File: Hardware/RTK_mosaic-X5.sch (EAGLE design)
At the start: 244 parts, among them J2 MAGJACK-POE, J3 MICRO-SD-PUSH-PUSH-EXT-PIN, J4 Vertical Qwiic Connector, J9 MAGJACK-POE, U1 ESP32-WROVER-IE, U10 POE_PSU-DP990X, U11 SN74AVC4T774PW, U17 URB2405YMD, U2 CH340C, U3 AP7361C-33FGEUDFN-8, U4 TXS0108, U5 TXS0108, U6 AP7361C-33FGEUDFN-8, U7 KSZ8041NL, U8 MOSAIC-X5X5, U9 KSZ8041NL

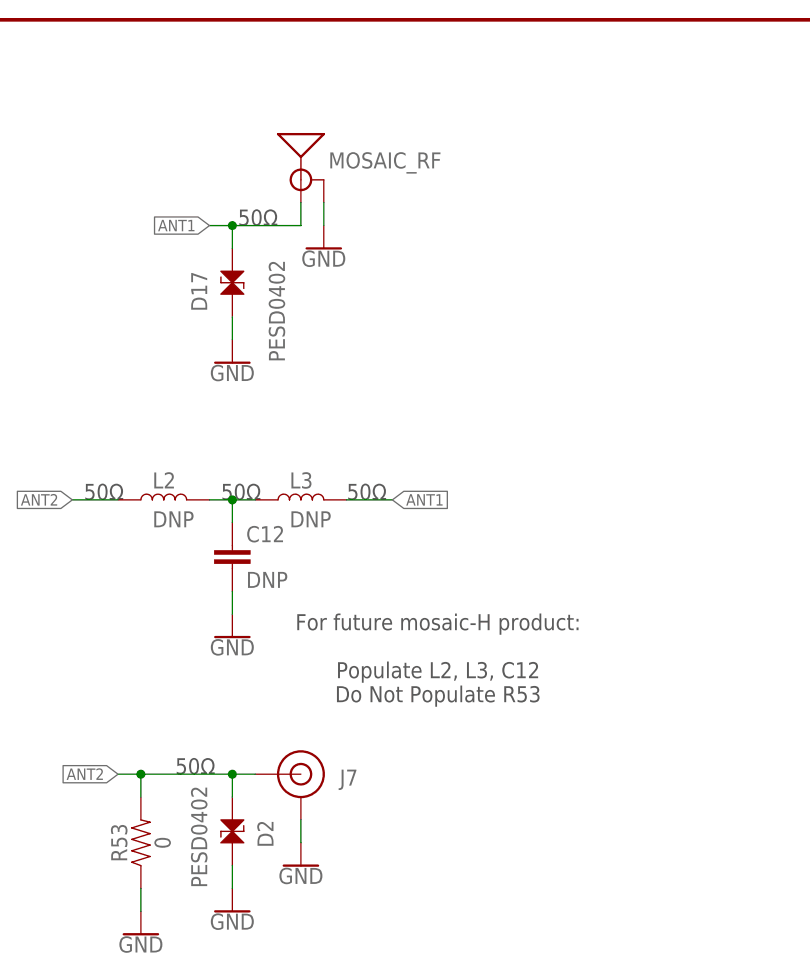
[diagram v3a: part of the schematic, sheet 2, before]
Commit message: Adding u.FL connector for mosaic-H - with standoff holes for a u.FL-SMA daughter board
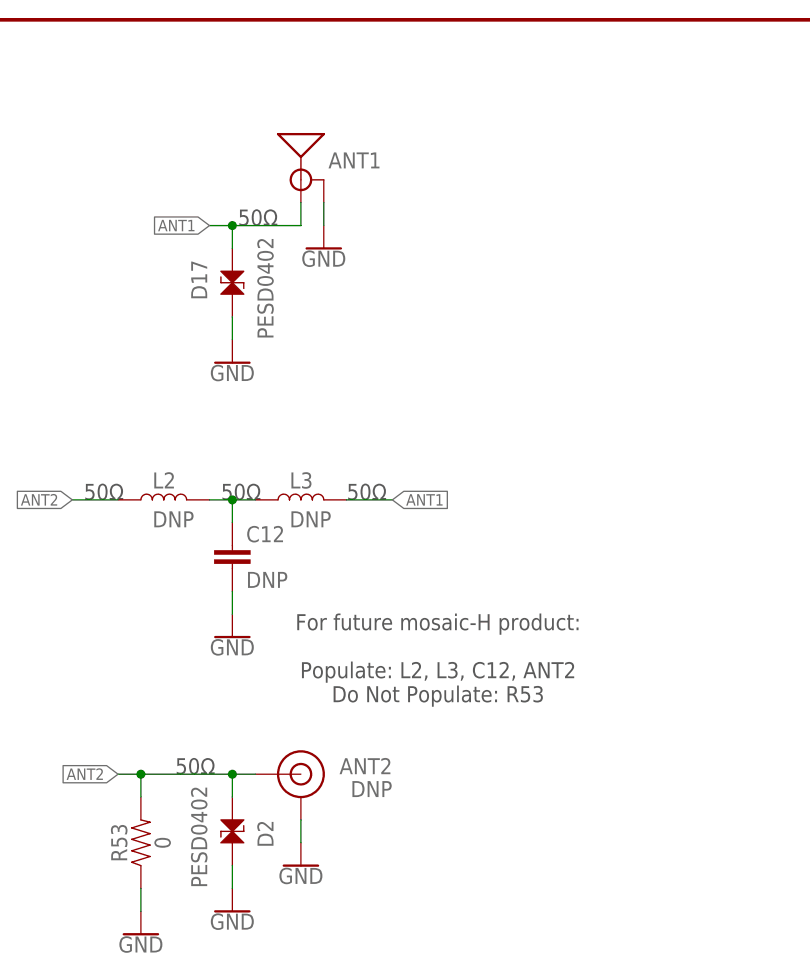
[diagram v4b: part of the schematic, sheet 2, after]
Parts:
- removed J7: (no value), SparkFun-Connectors:U.FL2PIN-REDUCED-FOOTPRINT
- added ANT2: DNP, SparkFun-Connectors:U.FL2PIN-REDUCED__DNP_NO_CREAM
- renumbered MOSAIC_RF to ANT1
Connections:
- net N$6 renamed VANT
- net ANT2: now also ANT2.SIGNAL; no longer J7.SIGNAL
- net GND: now also ANT2.GND; no longer J7.GND
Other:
- note added: "For future mosaic-H product: Populate: L2, L3, C12, ANT2 Do Not Populate: R53"
- note removed: "For future mosaic-H product: Populate L2, L3, C12 Do Not Populate R53"
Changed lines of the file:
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@@
 <part name="GND100" library="SparkFun-PowerSymbols" deviceset="GND" device=""/>
 <part name="GND99" library="SparkFun-PowerSymbols" deviceset="GND" device=""/>
-<part name="MOSAIC_RF" library="SparkFun-RF" deviceset="ANTENNA-SMA-GROUNDED" device="EDGE_SMA" value="ANTENNA-SMA-GROUNDEDEDGE_SMA"/>
+<part name="ANT1" library="SparkFun-RF" deviceset="ANTENNA-SMA-GROUNDED" device="EDGE_SMA" value="ANTENNA-SMA-GROUNDEDEDGE_SMA"/>
 <part name="D17" library="SparkFun-DiscreteSemi" deviceset="PESD0402" device="-0402" value="PESD0402"/>
 <part name="GND101" library="SparkFun-PowerSymbols" deviceset="GND" device=""/>
@@
 <part name="R52" library="SparkFun-Resistors" deviceset="0OHM" device="-0603-1/10W" value="0"/>
 <part name="1V8" library="SparkFun-Connectors" deviceset="TEST-POINT" device="POGO_PTH" value="TEST-POINTPOGO_PTH"/>
-<part name="J7" library="SparkFun-Connectors" deviceset="U.FL2PIN" device="-REDUCED-FOOTPRINT"/>
+<part name="ANT2" library="SparkFun-Connectors" deviceset="U.FL2PIN" device="-REDUCED__DNP_NO_CREAM" value="DNP"/>
 <part name="GND91" library="SparkFun-PowerSymbols" deviceset="GND" device=""/>
 <part name="D2" library="SparkFun-DiscreteSemi" deviceset="PESD0402" device="-0402" value="PESD0402"/>
@@
 <attribute name="NAME" x="193.548" y="270.51" size="1.778" layer="95" font="vector"/>
 </instance>
-<instance part="J8" gate="G$1" x="175.26" y="264.16" smashed="yes">
+<instance part="J8" gate="J1" x="175.26" y="264.16" smashed="yes">
 <attribute name="NAME" x="170.18" y="259.08" size="1.778" layer="95"/>
 <attribute name="VALUE" x="177.8" y="256.54" size="1.778" layer="96"/>
@@
 </segment>
 <segment>
-<pinref part="J8" gate="G$1" pin="GND"/>
+<pinref part="J8" gate="J1" pin="GND"/>
 <pinref part="GND59" gate="1" pin="GND"/>
 <wire x1="175.26" y1="259.08" x2="175.26" y2="256.54" width="0.1524" layer="91"/>
@@
 <net name="ESP32_RF" class="0">
 <segment>
-<pinref part="J8" gate="G$1" pin="SIGNAL"/>
+<pinref part="J8" gate="J1" pin="SIGNAL"/>
 <pinref part="ESP32_RF" gate="G$1" pin="SIGNAL"/>
 <wire x1="180.34" y1="264.16" x2="182.88" y2="264.16" width="0.1524" layer="91"/>
@@
 <text x="297.18" y="226.06" size="1.778" layer="97" font="vector">50Ω</text>
 <text x="307.34" y="213.36" size="1.778" layer="97" font="vector" align="top-center">For future mosaic-H product:
-Populate L2, L3, C12
-Do Not Populate R53</text>
+Populate: L2, L3, C12, ANT2
+Do Not Populate: R53</text>
 </plain>
 <instances>
@@
 <attribute name="VALUE" x="294.64" y="253.746" size="1.778" layer="96" font="vector" rot="MR0" align="top-center"/>
 </instance>
-<instance part="MOSAIC_RF" gate="G$1" x="292.1" y="261.62" smashed="yes">
+<instance part="ANT1" gate="G$1" x="292.1" y="261.62" smashed="yes">
 <attribute name="NAME" x="295.148" y="262.89" size="1.778" layer="95" font="vector"/>
 </instance>
 <instance part="D17" gate="D1" x="284.48" y="251.46" smashed="yes" rot="MR270">
-<attribute name="NAME" x="281.686" y="251.46" size="1.778" layer="95" font="vector" rot="MR270"/>
-<attribute name="VALUE" x="288.544" y="252.73" size="1.778" layer="96" font="vector" rot="MR270" align="top-left"/>
+<attribute name="NAME" x="281.686" y="252.73" size="1.778" layer="95" font="vector" rot="MR270"/>
+<attribute name="VALUE" x="287.274" y="255.27" size="1.778" layer="96" font="vector" rot="MR270" align="top-left"/>
 </instance>
 <instance part="GND101" gate="1" x="284.48" y="241.3" smashed="yes" rot="MR0">
@@
 </instance>
 <instance part="1V8" gate="G$1" x="167.64" y="182.88" smashed="yes" rot="R180"/>
-<instance part="J7" gate="G$1" x="292.1" y="195.58" smashed="yes" rot="MR0">
-<attribute name="NAME" x="298.45" y="194.31" size="1.778" layer="95" rot="MR0"/>
-<attribute name="VALUE" x="289.56" y="187.96" size="1.778" layer="96" rot="MR0"/>
+<instance part="ANT2" gate="J1" x="292.1" y="195.58" smashed="yes" rot="MR0">
+<attribute name="NAME" x="302.26" y="195.58" size="1.778" layer="95" rot="MR0"/>
+<attribute name="VALUE" x="302.26" y="193.04" size="1.778" layer="96" rot="MR0"/>
 </instance>
 <instance part="GND91" gate="1" x="292.1" y="185.42" smashed="yes">
@@
 </segment>
 <segment>
-<pinref part="MOSAIC_RF" gate="G$1" pin="GND"/>
+<pinref part="ANT1" gate="G$1" pin="GND"/>
 <pinref part="GND99" gate="1" pin="GND"/>
 <wire x1="294.64" y1="259.08" x2="294.64" y2="256.54" width="0.1524" layer="91"/>
@@
 </segment>
 <segment>
-<pinref part="J7" gate="G$1" pin="GND"/>
+<pinref part="ANT2" gate="J1" pin="GND"/>
 <pinref part="GND91" gate="1" pin="GND"/>
 <wire x1="292.1" y1="190.5" x2="292.1" y2="187.96" width="0.1524" layer="91"/>
@@
 </segment>
 <segment>
-<pinref part="MOSAIC_RF" gate="G$1" pin="SIGNAL"/>
+<pinref part="ANT1" gate="G$1" pin="SIGNAL"/>
 <wire x1="281.94" y1="256.54" x2="284.48" y2="256.54" width="0.1524" layer="91"/>
 <wire x1="284.48" y1="256.54" x2="292.1" y2="256.54" width="0.1524" layer="91"/>
@@
 </segment>
 </net>
-<net name="N$6" class="0">
+<net name="VANT" class="0">
 <segment>
 <pinref part="FB3" gate="G$1" pin="2"/>
@@
 </segment>
 <segment>
-<pinref part="J7" gate="G$1" pin="SIGNAL"/>
+<pinref part="ANT2" gate="J1" pin="SIGNAL"/>
 <wire x1="287.02" y1="195.58" x2="284.48" y2="195.58" width="0.1524" layer="91"/>
 <wire x1="284.48" y1="195.58" x2="274.32" y2="195.58" width="0.1524" layer="91"/>

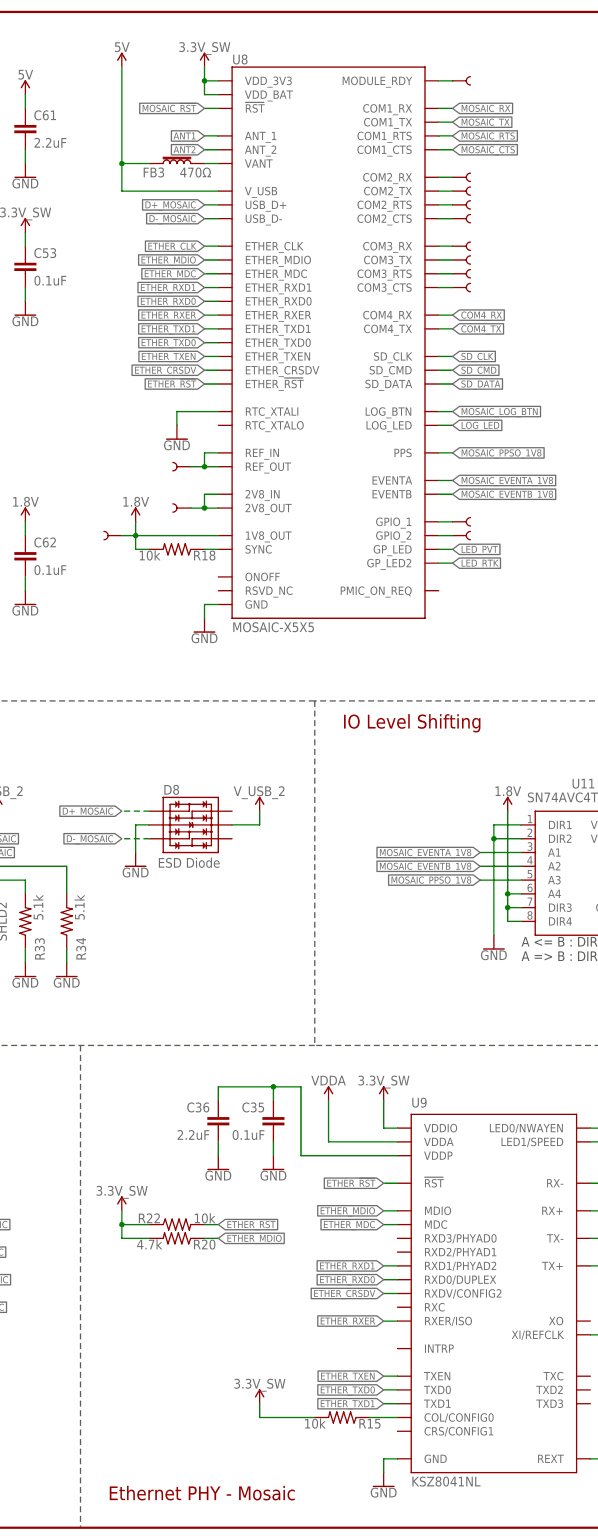
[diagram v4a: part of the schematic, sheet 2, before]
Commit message: Add Phy PROD_ID. Ready for manufacture
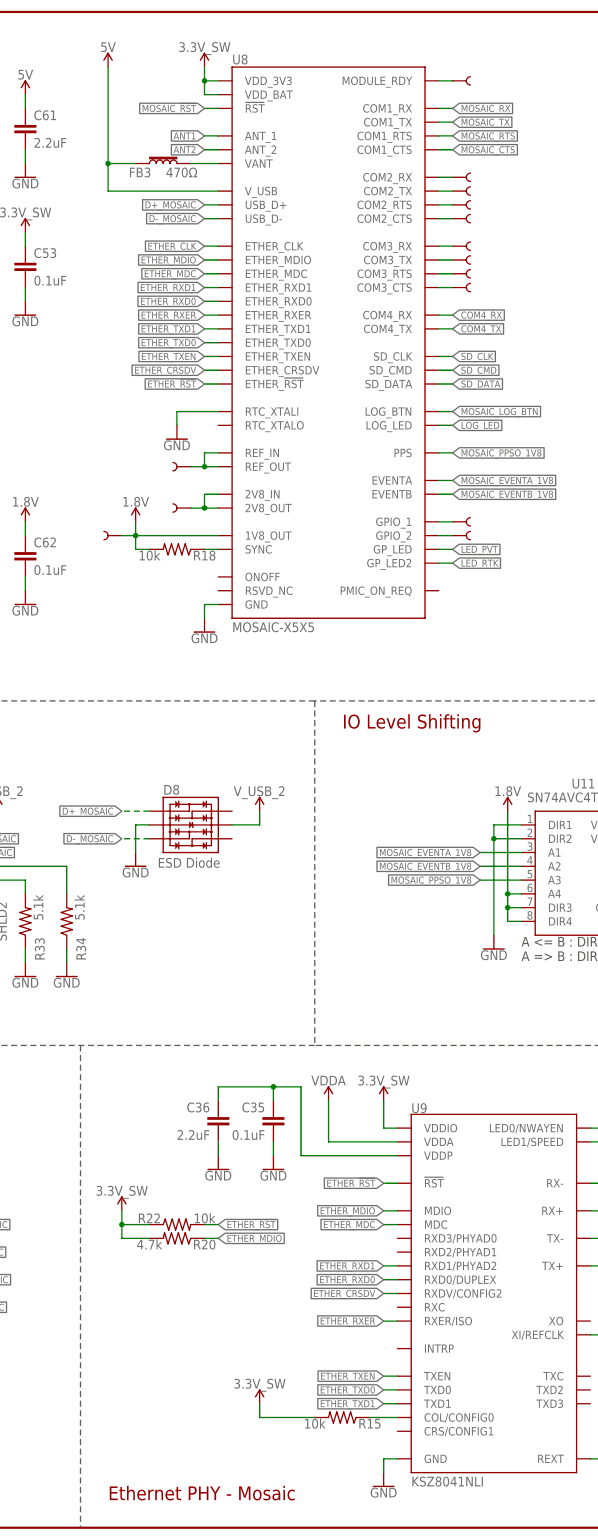
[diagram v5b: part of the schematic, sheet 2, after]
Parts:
- U7, U9: value KSZ8041NL -> KSZ8041NLI
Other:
- moved on the sheet: FB3
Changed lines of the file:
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@@
 <part name="C28" library="SparkFun-Capacitors" deviceset="0.1UF" device="-0603-25V-5%" value="0.1uF"/>
 <part name="GND62" library="SparkFun-PowerSymbols" deviceset="GND" device=""/>
-<part name="U7" library="Septentrio_mosaic-X5" deviceset="KSZ8041NL" device=""/>
+<part name="U7" library="Septentrio_mosaic-X5" deviceset="KSZ8041NL" device="" value="KSZ8041NLI"/>
 <part name="SUPPLY33" library="SparkFun-PowerSymbols" deviceset="3.3V" device=""/>
 <part name="SUPPLY38" library="SparkFun-PowerSymbols" deviceset="3.3V" device=""/>
@@
 <part name="C30" library="SparkFun-Capacitors" deviceset="0.1UF" device="-0603-25V-5%" value="0.1uF"/>
 <part name="GND41" library="SparkFun-PowerSymbols" deviceset="GND" device=""/>
-<part name="U9" library="Septentrio_mosaic-X5" deviceset="KSZ8041NL" device=""/>
+<part name="U9" library="Septentrio_mosaic-X5" deviceset="KSZ8041NL" device="" value="KSZ8041NLI"/>
 <part name="C35" library="SparkFun-Capacitors" deviceset="0.1UF" device="-0603-25V-5%" value="0.1uF"/>
 <part name="C36" library="SparkFun-Capacitors" deviceset="2.2UF" device="-0603-10V-20%" value="2.2uF"/>
@@
 </instance>
 <instance part="U7" gate="U1" x="215.9" y="78.74" smashed="yes">
-<attribute name="NAME" x="200.66" y="113.03" size="1.778" layer="95" font="vector"/>
+<attribute name="NAME" x="200.66" y="112.014" size="1.778" layer="95" font="vector"/>
 <attribute name="VALUE" x="200.66" y="43.18" size="1.778" layer="96" font="vector"/>
 </instance>
@@
 </instance>
 <instance part="U9" gate="U1" x="236.22" y="43.18" smashed="yes">
-<attribute name="NAME" x="220.98" y="77.47" size="1.778" layer="95" font="vector"/>
+<attribute name="NAME" x="220.98" y="76.454" size="1.778" layer="95" font="vector"/>
 <attribute name="VALUE" x="220.98" y="7.62" size="1.778" layer="96" font="vector"/>
 </instance>
@@
 <attribute name="VALUE" x="182.88" y="272.034" size="1.778" layer="96" align="bottom-center"/>
 </instance>
-<instance part="SUPPLY70" gate="G$1" x="167.64" y="269.24" smashed="yes">
-<attribute name="VALUE" x="167.64" y="272.034" size="1.778" layer="96" font="vector" align="bottom-center"/>
+<instance part="SUPPLY70" gate="G$1" x="165.1" y="269.24" smashed="yes">
+<attribute name="VALUE" x="165.1" y="272.034" size="1.778" layer="96" font="vector" align="bottom-center"/>
 </instance>
 <instance part="R17" gate="G$1" x="66.04" y="132.08" smashed="yes" rot="R90">
@@
 <attribute name="VALUE" x="137.16" y="188.214" size="1.778" layer="96" font="vector" align="bottom-center"/>
 </instance>
-<instance part="FB3" gate="G$1" x="177.8" y="251.46" smashed="yes" rot="R90">
-<attribute name="NAME" x="171.45" y="248.92" size="1.778" layer="95" font="vector"/>
-<attribute name="VALUE" x="184.15" y="248.92" size="1.778" layer="96" font="vector" rot="R180" align="top-left"/>
+<instance part="FB3" gate="G$1" x="175.26" y="251.46" smashed="yes" rot="R90">
+<attribute name="NAME" x="168.91" y="248.92" size="1.778" layer="95" font="vector"/>
+<attribute name="VALUE" x="181.61" y="248.92" size="1.778" layer="96" font="vector" rot="R180" align="top-left"/>
 </instance>
 <instance part="GND92" gate="1" x="149.86" y="248.92" smashed="yes">
@@
 <segment>
 <pinref part="SUPPLY70" gate="G$1" pin="5V"/>
-<wire x1="167.64" y1="246.38" x2="167.64" y2="251.46" width="0.1524" layer="91"/>
+<wire x1="165.1" y1="246.38" x2="165.1" y2="251.46" width="0.1524" layer="91"/>
 <pinref part="U8" gate="U1" pin="V_USB"/>
-<wire x1="167.64" y1="251.46" x2="167.64" y2="269.24" width="0.1524" layer="91"/>
-<wire x1="185.42" y1="246.38" x2="167.64" y2="246.38" width="0.1524" layer="91"/>
+<wire x1="165.1" y1="251.46" x2="165.1" y2="269.24" width="0.1524" layer="91"/>
+<wire x1="185.42" y1="246.38" x2="165.1" y2="246.38" width="0.1524" layer="91"/>
 <pinref part="FB3" gate="G$1" pin="1"/>
-<wire x1="172.72" y1="251.46" x2="167.64" y2="251.46" width="0.1524" layer="91"/>
-<junction x="167.64" y="251.46"/>
+<wire x1="170.18" y1="251.46" x2="165.1" y2="251.46" width="0.1524" layer="91"/>
+<junction x="165.1" y="251.46"/>
 </segment>
 <segment>
@@
 <pinref part="FB3" gate="G$1" pin="2"/>
 <pinref part="U8" gate="U1" pin="VANT"/>
-<wire x1="182.88" y1="251.46" x2="185.42" y2="251.46" width="0.1524" layer="91"/>
+<wire x1="180.34" y1="251.46" x2="185.42" y2="251.46" width="0.1524" layer="91"/>
 </segment>
 </net>
